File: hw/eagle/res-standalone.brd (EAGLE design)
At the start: 100 x 80 mm, 66 parts, among them IC2 7805T, IC3 L272M, IC4 L272M, IC5 STM32F415RGT, X5 22-23-2021

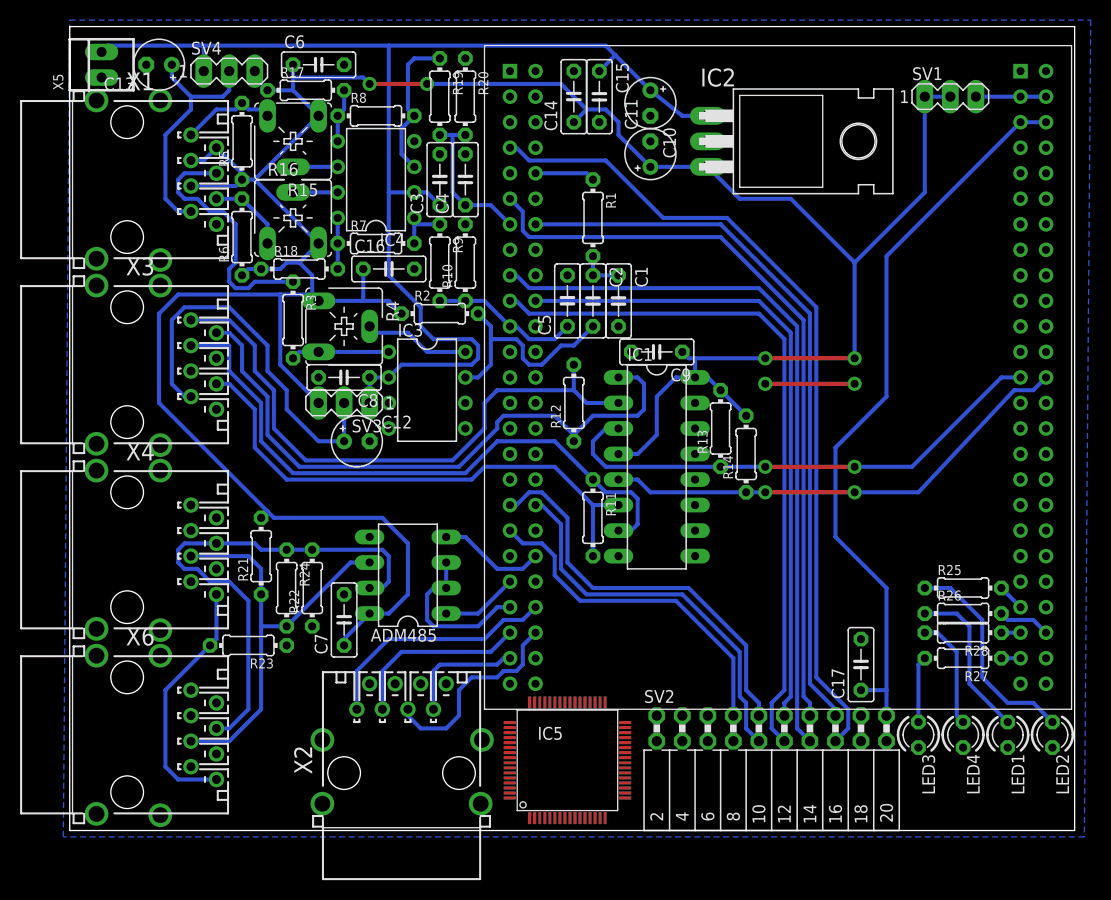
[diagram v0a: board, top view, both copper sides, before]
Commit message: slider gain offset
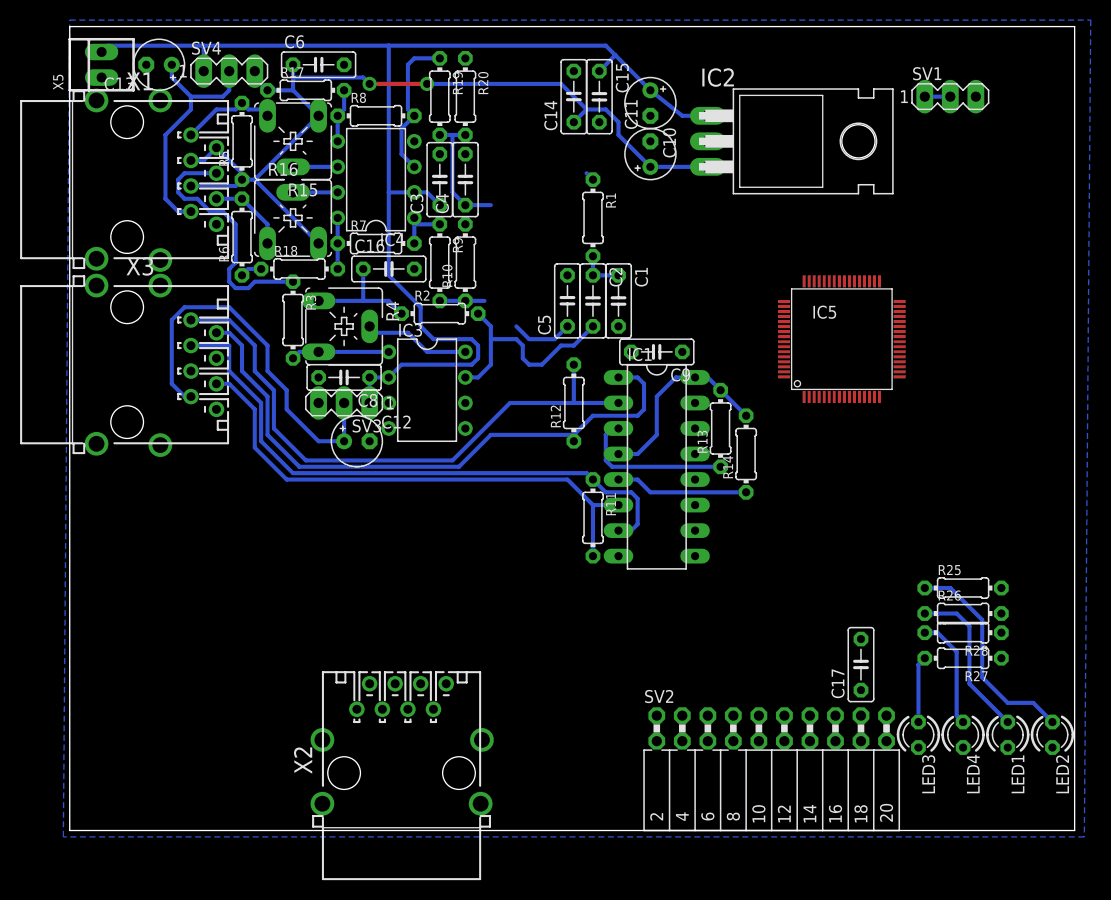
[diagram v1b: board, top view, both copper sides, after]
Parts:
- removed ADM485: (no value), ic-package:DIL08
- removed C7: (no value), rcl:C050-025X075
- removed R21, R22: 1k, resistor:0204/7
- removed R23: 100, resistor:0204/7
- removed R24: (no value), resistor:0204/7
- removed U$1: STM32F4-DISCOVERY, STM32F4-DISCOVERY:STM32F4-DISCOVERY
- removed X4, X6: (no value), con-appsys:RJ45
- moved IC5 50.0 mm to (76.8, 50.2)
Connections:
- removed net N$37: ADM485.4, U$1.P$40
- removed net N$41: ADM485.1, U$1.P$41
- removed net N$42: ADM485.2, ADM485.3, U$1.P$43
- removed net N$43: ADM485.6, R21.1, R24.2, X4.5, X6.5
- removed net N$44: ADM485.7, R22.2, R24.1, X4.4, X6.4
- removed net N$45: R23.2, X4.8, X6.8
- removed net N$47: R26.2, U$1.P$96
- removed net N$48: R27.1, U$1.P$97
- removed net N$49: R28.1, U$1.P$95
- removed net N$51: R25.2, U$1.P$93
- net +5V: no longer ADM485.8, C7.1, R21.2
- net CRS: no longer U$1.P$17
- net GND: no longer ADM485.5, C7.2, R22.1, R23.1, U$1.P$1, U$1.P$100, U$1.P$2, U$1.P$23, U$1.P$49, U$1.P$5, U$1.P$50, U$1.P$51, U$1.P$52, U$1.P$99
- net MDC: no longer U$1.P$7
- net MDIO: no longer U$1.P$14
- net N$14: no longer U$1.P$47
- net N$16: no longer U$1.P$44
- net N$18: no longer U$1.P$46
- net N$19: no longer U$1.P$45
- net N$20: no longer U$1.P$13
- net N$22: no longer U$1.P$75
- net N$23: no longer U$1.P$76
- net N$4: no longer U$1.P$10
- net N$40: no longer U$1.P$21
- net OSCIN: no longer U$1.P$11
- net RX1: no longer U$1.P$19
- net RXO: no longer U$1.P$20
- net TX1: no longer U$1.P$37
- net TXO: no longer U$1.P$36
- net TX_EN: no longer U$1.P$35
- net VCC: no longer U$1.P$53, U$1.P$54
- net VDD: no longer U$1.P$55, U$1.P$56
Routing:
- net +5V: track 287.9 -> 127.1 mm, vias 4 -> 2
- net MDC: track 82.1 -> 0.00 mm
- net OSCIN: track 75.0 -> 0.00 mm
- net VDD: track 76.4 -> 2.54 mm
- net CRS: track 72.5 -> 0.00 mm
- net MDIO: track 72.0 -> 0.00 mm
- net RX1: track 69.9 -> 0.00 mm
- net RXO: track 65.1 -> 0.00 mm
- net N$44: track 51.0 -> 0.00 mm
- net N$43: track 43.2 -> 0.00 mm
- net TX_EN: track 40.4 -> 0.00 mm
- net TXO: track 38.7 -> 0.00 mm
- net N$22: track 51.1 -> 15.8 mm, vias 2 -> 0
- net N$23: track 48.0 -> 13.2 mm, vias 2 -> 0
- net TX1: track 34.3 -> 0.00 mm
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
